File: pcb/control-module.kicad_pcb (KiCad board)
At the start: 2 copper layers, 50.3 x 37.8 mm, 64 parts, among them J1 Screw_Terminal_01x08, J2 Conn_01x06_Pin, J3 USB_C_Receptacle_USB2.0_16P, J4 Micro_SD_Card, J5 Screw_Terminal_01x02, Q1 SiS454DN, Q2 SiS454DN, Q3 SiS454DN, SW1 SW_DIP_x03, U1 TC2185-3.3VxCTTR, U2 USBLC6-2SC6, U3 STM32U545RETxQ, U4 MS5607-02BA, U5 LSM6DSL

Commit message: Syncing up!
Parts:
- J1: value Screw_Terminal_01x08 -> Screw_Terminal_01x06
- J2: value Conn_01x06_Pin -> Conn_01x07_Pin
- R11, R15, R19: value 1k -> 100k
- R12, R16, R20: value 1k -> 22k
- SW1: value SW_DIP_x03 -> SW_DIP_x04

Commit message: Updated Schematics
Completed Schematics for Test Bed, updated pcb
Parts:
- removed the C16 at (133.4, 58.1)
- removed the C2 at (154.2, 84.6)
- removed the C3 at (156.2, 84.6)
- removed J5: Screw_Terminal_01x02, TerminalBlock_Phoenix:TerminalBlock_Phoenix_MPT-0,5-2-2.54_1x02_P2.54mm_Horizontal
- removed the Q2 at (126.2, 62.5)
- removed the R13 at (126.2, 57.9)
- removed the R14 at (126.2, 59.4)
- removed the R15 at (128.8, 63.8)
- added BT1: Battery_Cell, Connector_JST:JST_PH_S2B-PH-K_1x02_P2.00mm_Horizontal, F.Cu at (208.6, 28.1)
- added C14: 10uF, Capacitor_SMD:C_0603_1608Metric_Pad1.08x0.95mm_HandSolder, F.Cu at (133.2, 58.1)
- added C18: 4.7uF, Capacitor_SMD:C_0603_1608Metric_Pad1.08x0.95mm_HandSolder, F.Cu at (203.4, 27.0)
- added C19: 1uF, Capacitor_SMD:C_0603_1608Metric_Pad1.08x0.95mm_HandSolder, F.Cu at (203.4, 29.5)
- added C20: 4.7uF, Capacitor_SMD:C_0603_1608Metric_Pad1.08x0.95mm_HandSolder, F.Cu at (203.4, 32.0)
- added C21: 1uF, Capacitor_SMD:C_0603_1608Metric_Pad1.08x0.95mm_HandSolder, F.Cu at (203.4, 34.5)
- added FID1: Fiducial, Fiducial:Fiducial_1mm_Mask2mm, F.Cu at (203.0, 47.1)
- added FID2: Fiducial, Fiducial:Fiducial_1mm_Mask2mm, F.Cu at (203.0, 50.6)
- added FID3: Fiducial, Fiducial:Fiducial_1mm_Mask2mm, F.Cu at (203.0, 54.2)
- added R17: 5.1k, Resistor_SMD:R_0603_1608Metric_Pad0.98x0.95mm_HandSolder, F.Cu at (203.4, 39.6)
- added R18: 5.1k, Resistor_SMD:R_0603_1608Metric_Pad0.98x0.95mm_HandSolder, F.Cu at (203.4, 42.1)
- added R2: 100k, Resistor_SMD:R_0603_1608Metric_Pad0.98x0.95mm_HandSolder, F.Cu at (245.6, 29.2)
- added R4: 10k, Resistor_SMD:R_0603_1608Metric, F.Cu at (210.5, 56.7)
- added TP_3V3_mcu1: TestPoint, TestPoint:TestPoint_Loop_D2.54mm_Drill1.5mm_Beaded, F.Cu at (203.8, 63.8)
- added TP_3V3_reg1: TestPoint, TestPoint:TestPoint_Loop_D2.54mm_Drill1.5mm_Beaded, F.Cu at (214.2, 78.0)
- added TP_3V3_sd1: TestPoint, TestPoint:TestPoint_Loop_D2.54mm_Drill1.5mm_Beaded, F.Cu at (224.4, 47.9)
- added TP_ADC_BAT_DIV1: TestPoint, TestPoint:TestPoint_Loop_D2.54mm_Drill1.5mm_Beaded, F.Cu at (203.8, 68.8)
- added TP_BARO_CS1: TestPoint, TestPoint:TestPoint_Loop_D2.54mm_Drill1.5mm_Beaded, F.Cu at (191.7, 28.3)
- added TP_BARO_MISO1: TestPoint, TestPoint:TestPoint_Loop_D2.54mm_Drill1.5mm_Beaded, F.Cu at (191.7, 33.3)
- added TP_BARO_MOSI1: TestPoint, TestPoint:TestPoint_Loop_D2.54mm_Drill1.5mm_Beaded, F.Cu at (191.7, 38.4)
- added TP_BARO_SCK1: TestPoint, TestPoint:TestPoint_Loop_D2.54mm_Drill1.5mm_Beaded, F.Cu at (191.7, 43.4)
- added TP_BATT1: TestPoint, TestPoint:TestPoint_Loop_D2.54mm_Drill1.5mm_Beaded, F.Cu at (207.3, 52.9)
- added TP_BAT_SENSE_MID1: TestPoint, TestPoint:TestPoint_Loop_D2.54mm_Drill1.5mm_Beaded, F.Cu at (212.3, 47.9)
- added TP_BOOT1: TestPoint, TestPoint:TestPoint_Loop_D2.54mm_Drill1.5mm_Beaded, F.Cu at (208.8, 63.8)
- added TP_GND_1: TestPoint, TestPoint:TestPoint_Loop_D2.54mm_Drill1.5mm_Beaded, F.Cu at (212.3, 52.9)
- added TP_GND_2: TestPoint, TestPoint:TestPoint_Loop_D2.54mm_Drill1.5mm_Beaded, F.Cu at (217.4, 47.9)
- added TP_IMU_INT1: TestPoint, TestPoint:TestPoint_Loop_D2.54mm_Drill1.5mm_Beaded, F.Cu at (191.7, 48.5)
- added TP_IMU_INT2: TestPoint, TestPoint:TestPoint_Loop_D2.54mm_Drill1.5mm_Beaded, F.Cu at (196.7, 28.3)
- added TP_NRST1: TestPoint, TestPoint:TestPoint_Loop_D2.54mm_Drill1.5mm_Beaded, F.Cu at (208.8, 68.8)
- added TP_PYRO1_CONT1: TestPoint, TestPoint:TestPoint_Loop_D2.54mm_Drill1.5mm_Beaded, F.Cu at (191.7, 55.5)
- added TP_PYRO1_FIRE1: TestPoint, TestPoint:TestPoint_Loop_D2.54mm_Drill1.5mm_Beaded, F.Cu at (191.7, 60.6)
- added TP_PYRO1_GNDD1: TestPoint, TestPoint:TestPoint_Loop_D2.54mm_Drill1.5mm_Beaded, F.Cu at (191.7, 65.6)
- added TP_PYRO1_OUT1: TestPoint, TestPoint:TestPoint_Loop_D2.54mm_Drill1.5mm_Beaded, F.Cu at (191.7, 70.7)
- added TP_PYRO2_CONT1: TestPoint, TestPoint:TestPoint_Loop_D2.54mm_Drill1.5mm_Beaded, F.Cu at (231.5, 47.9)
- added TP_PYRO2_FIRE1: TestPoint, TestPoint:TestPoint_Loop_D2.54mm_Drill1.5mm_Beaded, F.Cu at (231.5, 52.9)
- added TP_PYRO2_GNDD1: TestPoint, TestPoint:TestPoint_Loop_D2.54mm_Drill1.5mm_Beaded, F.Cu at (231.5, 58.0)
- added TP_PYRO2_OUT1: TestPoint, TestPoint:TestPoint_Loop_D2.54mm_Drill1.5mm_Beaded, F.Cu at (231.5, 63.0)
- added TP_Power_Mux_STAT1: TestPoint, TestPoint:TestPoint_Loop_D2.54mm_Drill1.5mm_Beaded, F.Cu at (217.4, 52.9)
- added TP_SD_CLK1: TestPoint, TestPoint:TestPoint_Loop_D2.54mm_Drill1.5mm_Beaded, F.Cu at (224.4, 52.9)
- added TP_SD_CMD1: TestPoint, TestPoint:TestPoint_Loop_D2.54mm_Drill1.5mm_Beaded, F.Cu at (224.4, 58.0)
- added TP_SD_DAT1: TestPoint, TestPoint:TestPoint_Loop_D2.54mm_Drill1.5mm_Beaded, F.Cu at (224.4, 63.0)
- added TP_SD_EJECT1: TestPoint, TestPoint:TestPoint_Loop_D2.54mm_Drill1.5mm_Beaded, F.Cu at (213.8, 63.8)
- added TP_SPI_CS1: TestPoint, TestPoint:TestPoint_Loop_D2.54mm_Drill1.5mm_Beaded, F.Cu at (196.7, 33.3)
- added TP_SPI_MISO1: TestPoint, TestPoint:TestPoint_Loop_D2.54mm_Drill1.5mm_Beaded, F.Cu at (196.7, 38.4)
- added TP_SPI_MOSI1: TestPoint, TestPoint:TestPoint_Loop_D2.54mm_Drill1.5mm_Beaded, F.Cu at (196.7, 43.4)
- added TP_SPI_SCK1: TestPoint, TestPoint:TestPoint_Loop_D2.54mm_Drill1.5mm_Beaded, F.Cu at (196.7, 48.5)
- added TP_USB_D+1: TestPoint, TestPoint:TestPoint_Loop_D2.54mm_Drill1.5mm_Beaded, F.Cu at (223.2, 28.3)
- added TP_USB_D-1: TestPoint, TestPoint:TestPoint_Loop_D2.54mm_Drill1.5mm_Beaded, F.Cu at (223.2, 33.3)
- added TP_VUSB1: TestPoint, TestPoint:TestPoint_Loop_D2.54mm_Drill1.5mm_Beaded, F.Cu at (213.8, 68.8)
- added TP_V_USB1: TestPoint, TestPoint:TestPoint_Loop_D2.54mm_Drill1.5mm_Beaded, F.Cu at (223.2, 38.4)
- added TP_V_{BAT}1: TestPoint, TestPoint:TestPoint_Loop_D2.54mm_Drill1.5mm_Beaded, F.Cu at (240.9, 28.0)
- added TP_V_{mux}1: TestPoint, TestPoint:TestPoint_Loop_D2.54mm_Drill1.5mm_Beaded, F.Cu at (240.9, 33.1)
- added U6: MCP73831-2-OT, Package_TO_SOT_SMD:SOT-23-5, F.Cu at (216.1, 28.2)
- added U7: MIC5504-3.3YM5, Package_TO_SOT_SMD:SOT-23-5, F.Cu at (216.1, 32.8)
- C1: value 1uF -> 100nF; footprint Capacitor_SMD:C_0603_1608Metric -> Capacitor_SMD:C_0603_1608Metric_Pad1.08x0.95mm_HandSolder
- D3: value VS5V0UA1LAMTR -> LED; footprint Diode_SMD:D_SOD-128 -> LED_SMD:LED_0603_1608Metric_Pad1.05x0.95mm_HandSolder
- D4: value B350A-13-F -> LED; footprint Diode_SMD:D_SOD-123F -> LED_SMD:LED_0603_1608Metric_Pad1.05x0.95mm_HandSolder
- R1: value 1k -> 300k; footprint Resistor_SMD:R_0603_1608Metric -> Resistor_SMD:R_0603_1608Metric_Pad0.98x0.95mm_HandSolder
- R16: value 22k -> 5.1k
- U1: value TC2185-3.3VxCTTR -> TPS2116DRL; footprint Package_TO_SOT_SMD:SOT-23-5 -> Package_TO_SOT_SMD:SOT-583-8
- moved R1 131.1 mm to (245.6, 26.7)
- moved C1 92.2 mm to (227.9, 27.0), turned to 0 degrees
- moved D4 88.7 mm to (207.8, 39.3)
- moved R16 77.9 mm to (203.4, 37.0), turned to 0 degrees
- moved D3 66.5 mm to (207.8, 36.7), turned to 0 degrees
- moved U1 56.5 mm to (206.6, 57.4), turned to 0 degrees
- moved J4 0.09 mm to (142.1, 59.6)
- renumbered C12 to C10, C13 to C11, C14 to C12, C15 to C13, C17 to C15, C18 to C16, C19 to C17, C4 to C2, C5 to C3, C6 to C4, C7 to C5, C8 to C6, C9 to C7, C10 to C8, C11 to C9, Q3 to Q2, R11 to R10, R12 to R11, R17 to R12, R18 to R13, R19 to R14, R20 to R15, R2 to R3, R3 to R5, R7 to R6, R8 to R7, R9 to R8, R10 to R9
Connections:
- C1 pad 1: /V_USB -> +5V_USB
- C13 pad 1: /V_USB -> +3.3V
- D3 pad 1: /V_USB -> Net-(D3-K)
- D3 pad 2: GNDD -> +5V_USB
- D4 pad 1: /Recovery Power -> Net-(D4-K)
- D4 pad 2: /Valve Controller/Out -> /Battery/Status
- J1 pad 1: /Valve Controller/Out -> +3.3V
- J1 pad 2: /Recovery Power -> Net-(J1-Pin_2)
- J1 pad 4: /Recovery Power -> Net-(J1-Pin_2)
- J1 pad 6: /Recovery Power -> Net-(J1-Pin_2)
- J2 pad 1: +12V -> GNDA
- J2 pad 2: +12V -> GNDA
- J3 pad A4: /V_USB -> +5V_USB
- J3 pad A9: /V_USB -> +5V_USB
- J3 pad B4: /V_USB -> +5V_USB
- J3 pad B9: /V_USB -> +5V_USB
- R1 pad 1: GNDD -> Net-(U1-PR1)
- R1 pad 2: /Recovery Power -> /V_USB
- R16 pad 1: GNDD -> /Battery/Program
- R16 pad 2: /MCU/ADC1_IN15 -> GNDD
- R3 pad 1: /V_USB -> +5V_USB
- U1 pad 1: /V_USB -> GNDD
- U1 pad 2: GNDD -> /V_{mux}
- U1 pad 4: Net-(U1-BP) -> Net-(U1-PR1)
- U1 pad 5: +3.3V -> /V_USB
- U2 pad 4: /MCU/USB_DP -> /USB-C/USB_D+
- U2 pad 6: /MCU/USB_DN -> /USB-C/USB_D-
- U3 pad 2: /MCU/VALVE_FIRE -> unconnected-(U3-PC13-Pad2)
- U3 pad 24: /MCU/ADC1_IN15 -> unconnected-(U3-PB0-Pad24)
- U3 pad 48: /V_USB -> +3.3V
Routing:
- net unconnected-(U3-PB0-Pad24): track 0.00 -> 29.6 mm, vias 0 -> 2
- net /MCU/ADC1_IN15: track 29.6 -> 0.00 mm, vias 2 -> 0
- net unconnected-(U3-PC13-Pad2): track 0.00 -> 19.6 mm, vias 0 -> 2
- net /MCU/VALVE_FIRE: track 19.6 -> 0.00 mm, vias 2 -> 0
- net +3.3V: track 1.92 -> 19.7 mm
- net /Valve Controller/Out: track 12.9 -> 0.00 mm
- net /V_USB: track 12.6 -> 7.71 mm
- net Net-(U1-BP): track 1.92 -> 0.00 mm
- net (no net): track 0.00 -> 1.92 mm
- net Net-(Q2-G): track 1.66 -> 3.29 mm
- net Net-(Q2-G) (its old number): track 1.63 -> 0.00 mm
- added copper zone on F.Cu, net Net-(J1-Pin_2)
- removed copper zone on F.Cu, net +12V
- removed copper zone on F.Cu, net /Recovery Power

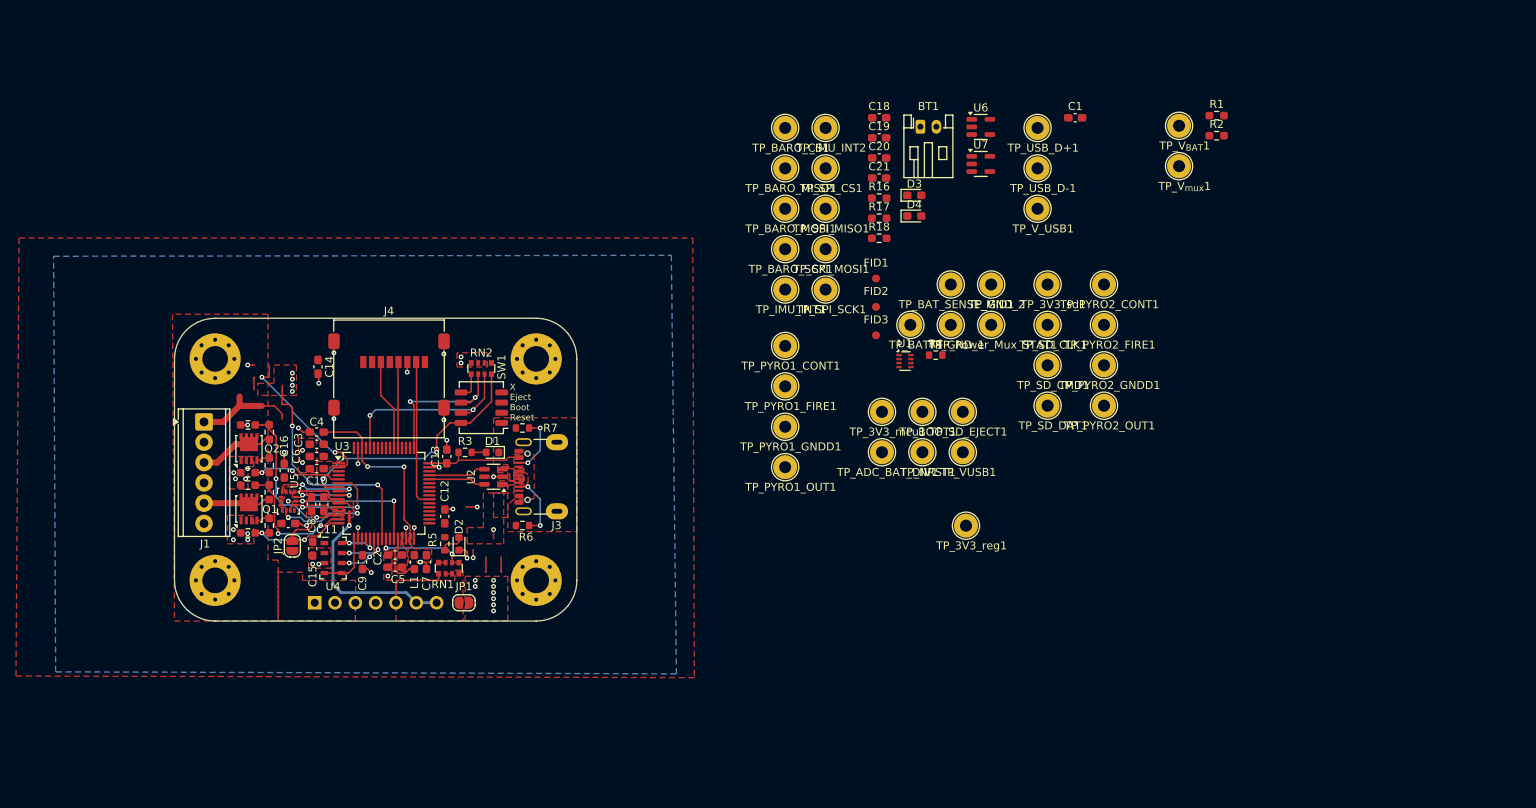
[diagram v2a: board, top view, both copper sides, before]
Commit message: Updated Board size
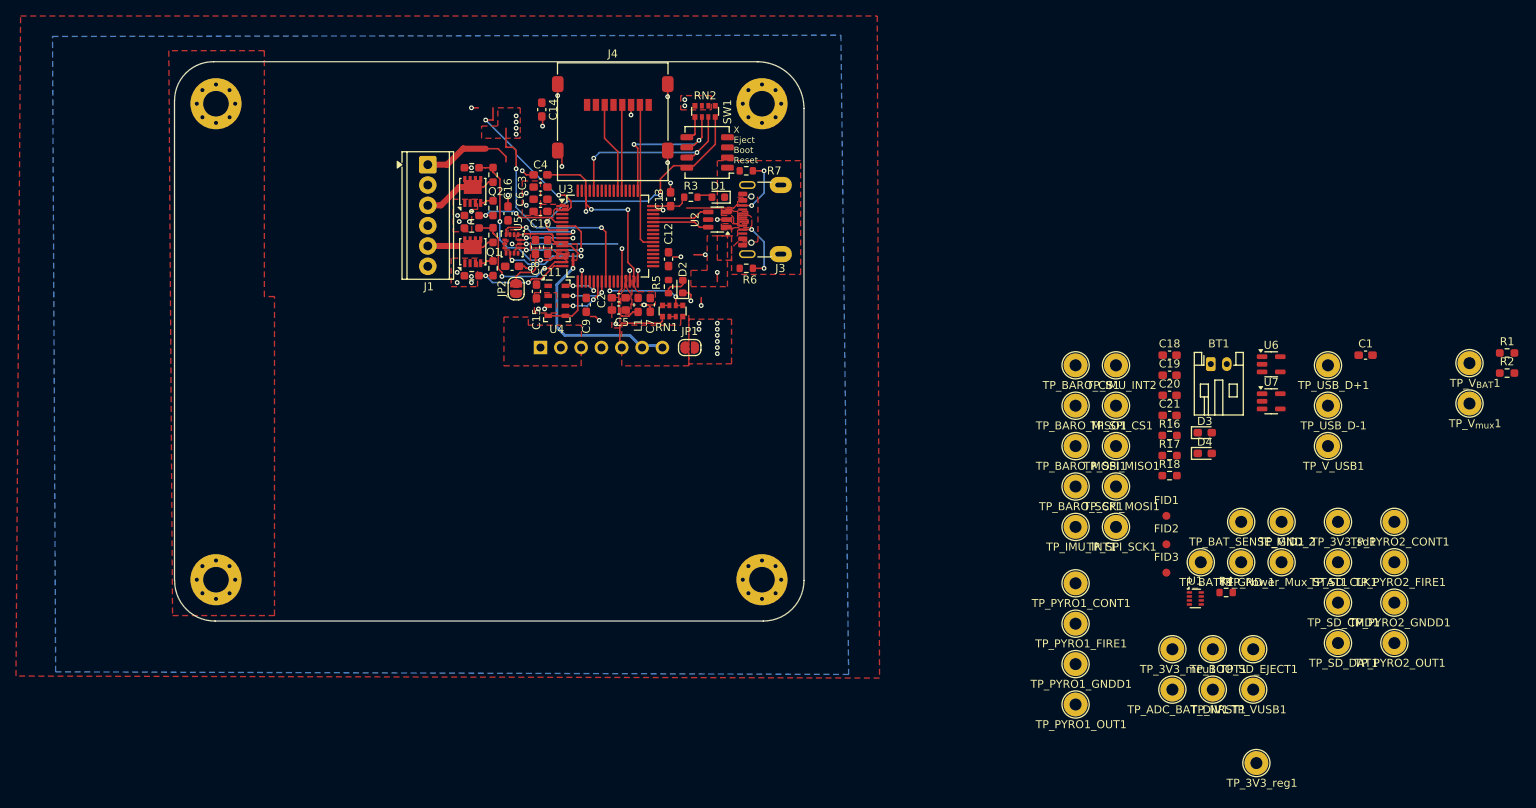
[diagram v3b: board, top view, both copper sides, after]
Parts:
- moved D3 46.9 mm to (244.1, 66.4)
- moved FID3 46.9 mm to (239.3, 83.9)
- moved TP_3V3_reg1 46.9 mm to (250.6, 107.7)
- moved TP_ADC_BAT_DIV1 46.9 mm to (240.1, 98.5)
- moved TP_IMU_INT2 46.9 mm to (233.0, 58.0)
- moved TP_PYRO2_GNDD1 46.9 mm to (267.8, 87.6)
- moved TP_PYRO2_OUT1 46.9 mm to (267.8, 92.7)
- moved TP_SD_CMD1 46.9 mm to (260.8, 87.6)
- moved TP_SD_DAT1 46.9 mm to (260.8, 92.7)
- moved TP_SPI_CS1 46.9 mm to (233.0, 63.0)
- moved TP_SPI_SCK1 46.9 mm to (233.0, 78.2)
- moved TP_USB_D+1 46.9 mm to (259.5, 58.0)
- moved TP_USB_D-1 46.9 mm to (259.5, 63.0)
- moved TP_VUSB1 46.9 mm to (250.2, 98.5)
- moved TP_V_{BAT}1 46.9 mm to (277.2, 57.7)
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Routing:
- net Net-(J3-CC2): track 7.50 -> 15.2 mm
- net /V_USB: track 7.71 -> 0.00 mm
- net /IMU Sensors/imu_sclk: track 16.8 -> 12.1 mm, vias 2 -> 1
- net Net-(U3-VLXSMPS): track 6.88 -> 11.6 mm, vias 0 -> 1
- net +3.3V: track 19.7 -> 16.6 mm
- net /MCU/VDD11: track 23.1 -> 25.1 mm, vias 2 -> 3
- net GNDD: track 34.3 -> 32.3 mm, vias 53 -> 52
- net (no net): track 1.92 -> 0.00 mm
- net Net-(Q2-G): track 3.29 -> 1.66 mm
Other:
- board size 50.3 x 37.8 mm -> 78.7 x 69.9 mm
